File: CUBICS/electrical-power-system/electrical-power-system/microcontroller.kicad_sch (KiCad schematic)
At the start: 13 parts, among them J401 Conn_01x02, U401 TCAN1043xDxQ1, U402 ATmega328-P, U403 FXMA108

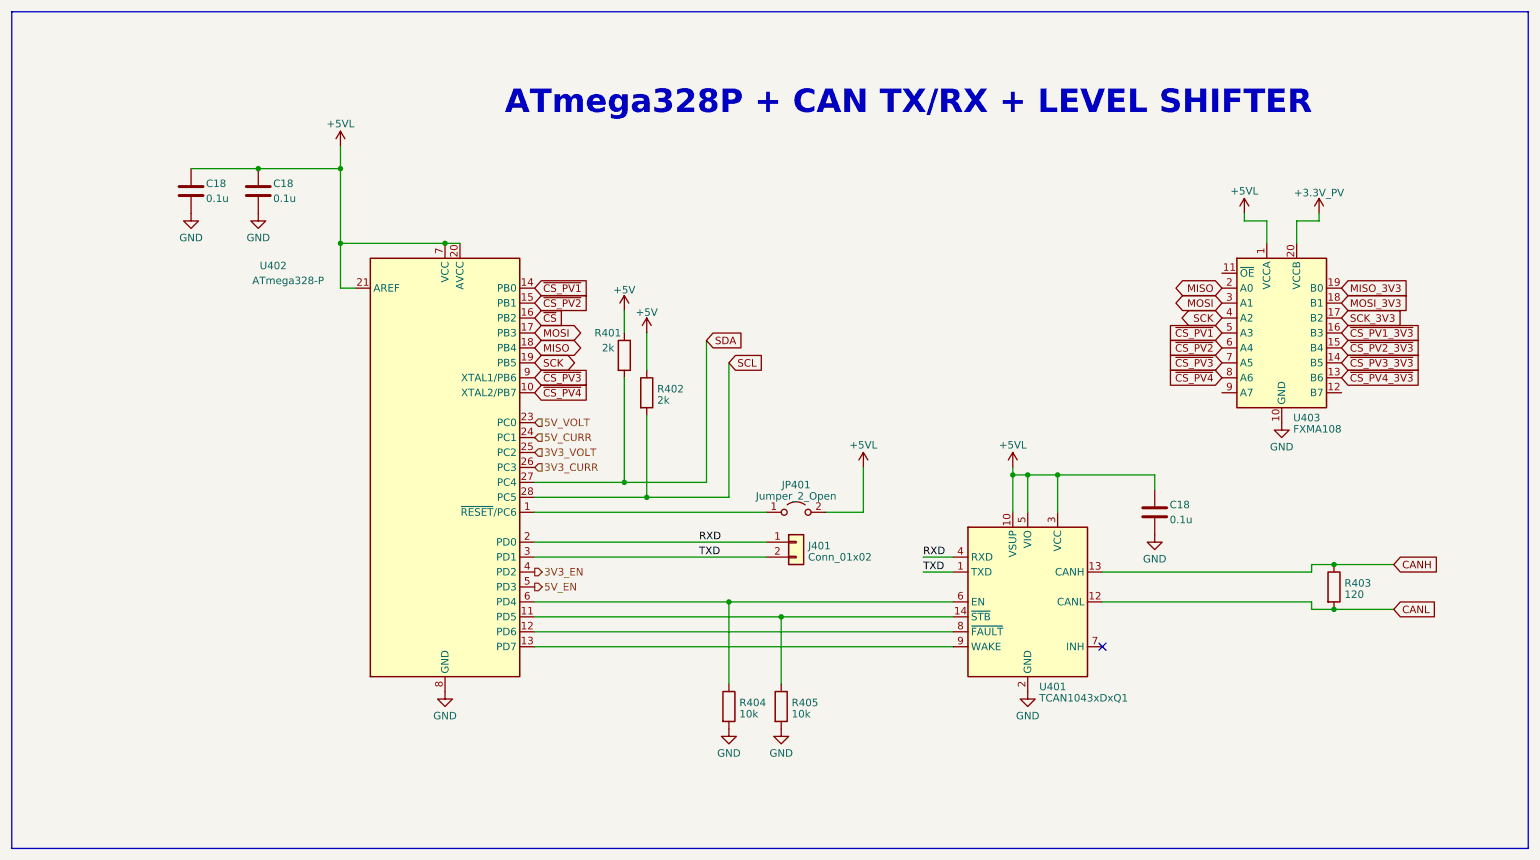
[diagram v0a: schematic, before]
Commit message: rev 1.0 routing complete updated schematic
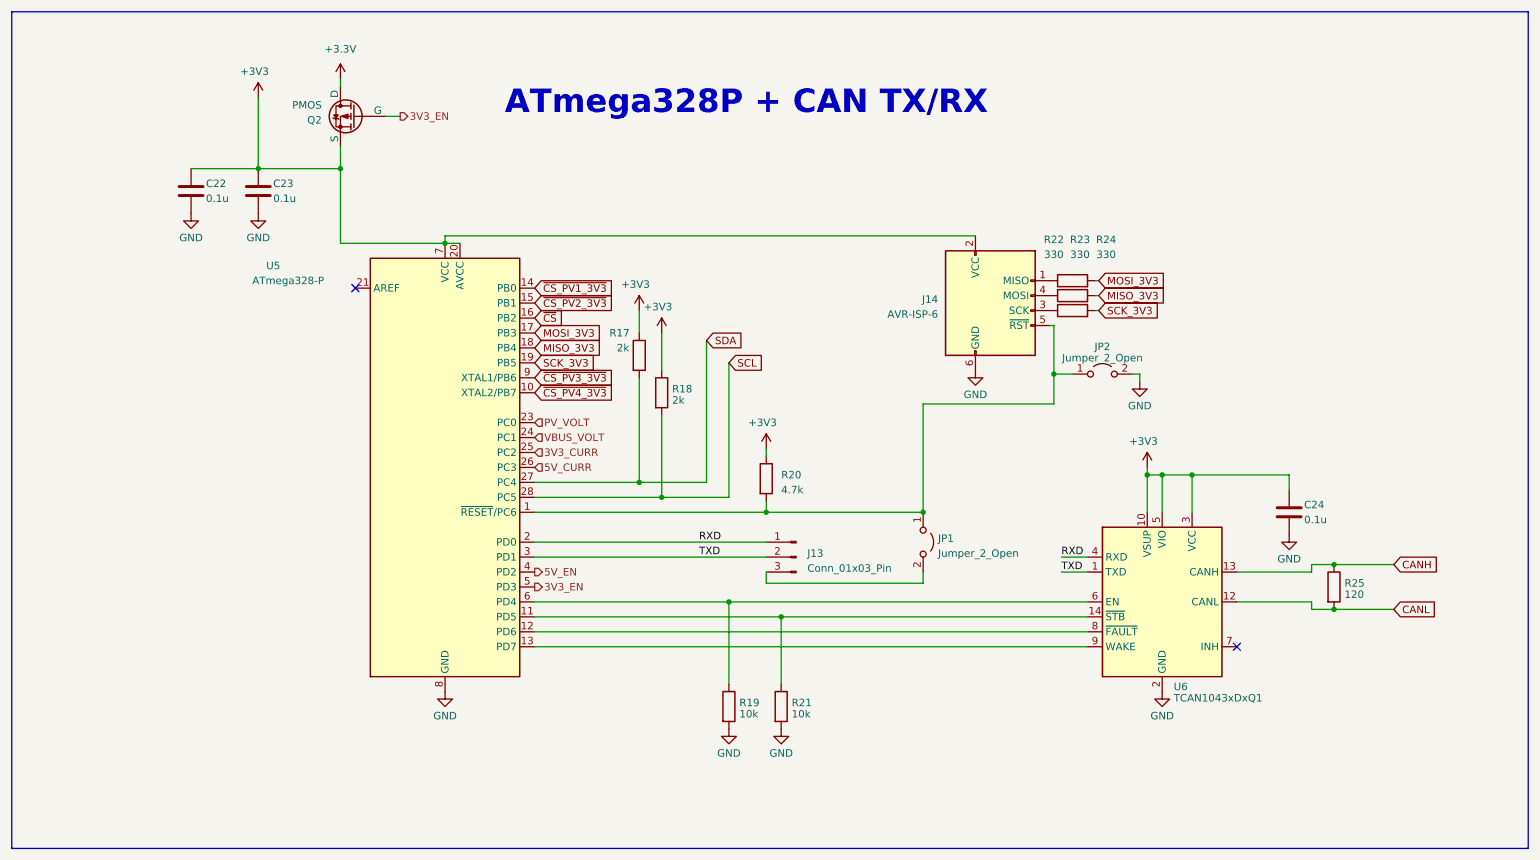
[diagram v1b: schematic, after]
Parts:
- removed J401: Conn_01x02, Connector_Phoenix_MC:PhoenixContact_MCV_1,5_2-G-3.81_1x02_P3.81mm_Vertical, symbol Connector_Generic:Conn_01x02
- removed U403: FXMA108, Package_DFN_QFN:WQFN-20-1EP_2.5x4.5mm_P0.5mm_EP1x2.9mm, symbol Logic_LevelTranslator:FXMA108
- added J13: Conn_01x03_Pin, Connector_PinHeader_2.54mm:PinHeader_1x03_P2.54mm_Vertical, symbol Connector:Conn_01x03_Pin
- added J14: AVR-ISP-6, Connector_PinHeader_2.54mm:PinHeader_2x03_P2.54mm_Vertical, symbol Connector:AVR-ISP-6
- added JP1: Jumper_2_Open, Resistor_SMD:R_0603_1608Metric, symbol Jumper:Jumper_2_Open
- added Q2: PMOS, Package_TO_SOT_SMD:SOT-23, symbol Simulation_SPICE:PMOS
- added R20: 4.7k, Resistor_SMD:R_0603_1608Metric, symbol Device:R
- added R22, R23, R24: 330, Resistor_SMD:R_0603_1608Metric, symbol Device:R
- JP2: renamed from JP401; footprint (none) -> Resistor_SMD:R_0603_1608Metric
- R17: renamed from R401; footprint (none) -> Resistor_SMD:R_0603_1608Metric
- R18: renamed from R402; footprint (none) -> Resistor_SMD:R_0603_1608Metric
- R19: renamed from R404; footprint (none) -> Resistor_SMD:R_0603_1608Metric
- R21: renamed from R405; footprint (none) -> Resistor_SMD:R_0603_1608Metric
- R25: renamed from R403; footprint (none) -> Resistor_SMD:R_0603_1608Metric
- renumbered C18 to C22, C18 to C23, C18 to C24, U402 to U5, U401 to U6
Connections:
- net 3V3_VOLT is gone; now on net 3V3_CURR: U5.25 (PC2)
- net MISO is gone; now on net MISO_3V3: U5.18 (PB4)
- net MOSI is gone; now on net MOSI_3V3: U5.17 (PB3)
- net SCK is gone; now on net SCK_3V3: U5.19 (PB5)
- net ~{CS_PV1} is gone; now on net ~{CS_PV1_3V3}: U5.14 (PB0)
- net ~{CS_PV2} is gone; now on net ~{CS_PV2_3V3}: U5.15 (PB1)
- net ~{CS_PV3} is gone; now on net ~{CS_PV3_3V3}: U5.9 (XTAL1/PB6)
- net ~{CS_PV4} is gone; now on net ~{CS_PV4_3V3}: U5.10 (XTAL2/PB7)
- net +3.3V: now also Q2.1 (D)
- net 3V3_CURR: no longer U5.26 (PC3)
- net 3V3_EN: now also U5.5 (PD3), Q2.2 (G); no longer U5.4 (PD2)
- net 5V_CURR: now also U5.26 (PC3); no longer U5.24 (PC1)
- net 5V_EN: now also U5.4 (PD2); no longer U5.5 (PD3)
- net GND: now also JP2.2 (B), J14.6 (GND)
- net MISO_3V3: now also R23.2
- net MOSI_3V3: now also R22.2
- net RXD: now also J13.1 (Pin_1)
- net SCK_3V3: now also R24.2
- net TXD: now also J13.2 (Pin_2)
- net at JP2.1 (A), U5.1 (~{RESET}/PC6): now also J14.5 (~{RST}), JP1.1 (A), R20.2
- net +5V renamed +3V3
- net +3V3: now also C22.1, C23.1, C24.1, U5.20 (AVCC), U5.7 (VCC), U6.10 (VSUP), U6.3 (VCC), U6.5 (VIO), J14.2 (VCC), Q2.3 (S), R20.1
- removed net +5VL: C22.1, C23.1, C24.1, JP2.2 (B), U5.20 (AVCC), U5.21 (AREF), U5.7 (VCC), U6.10 (VSUP), U6.3 (VCC), U6.5 (VIO)
- net 5V_VOLT renamed PV_VOLT
- new net: J13.3 (Pin_3), JP1.2 (B)
- new net: J14.4 (MOSI), R23.1
- new net: J14.3 (SCK), R24.1
- new net: J14.1 (MISO), R22.1
- new net VBUS_VOLT: U5.24 (PC1)
- no-connect marks 1 -> 2
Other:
- note added: "ATmega328P + CAN TX/RX"
- note removed: "ATmega328P + CAN TX/RX + LEVEL SHIFTER"
- moved on the sheet: C24, JP2, R17, R18, U6
